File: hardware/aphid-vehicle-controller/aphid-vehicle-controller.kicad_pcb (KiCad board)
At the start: 4 copper layers, 135 parts, among them J1 MONITOR UART, J2 ModICE ME-MX 24, J3 MAIN_DEBUG, J4 MONITOR_DEBUG, U1 STM32G491CETx, U2 AMS1117-3.3, U3 LMR33630BDDA, U4 TJA1042T-3, U5 TJA1042T-3, U6 TJA1042T-3, U7 STM32G431KBTx, U8 BTS6143D, Y1 8 MHz, Y2 8 MHz

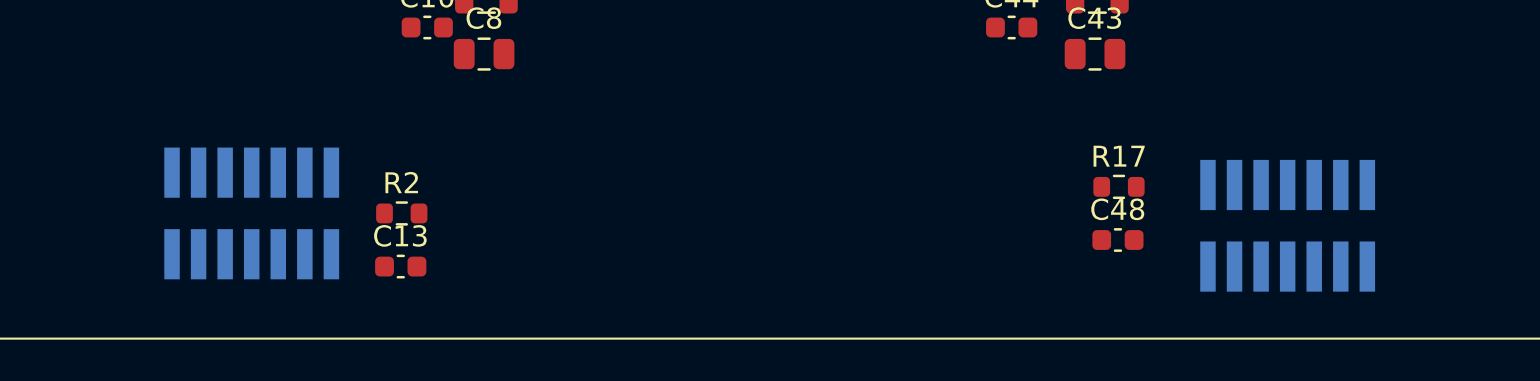
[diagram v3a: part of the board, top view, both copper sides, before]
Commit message: Changed debug connector to tagconnect
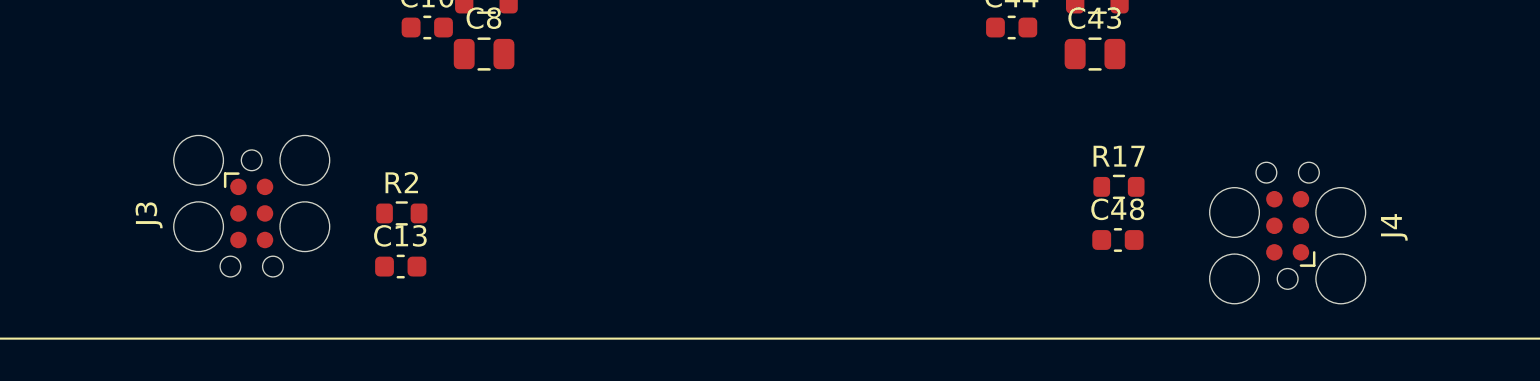
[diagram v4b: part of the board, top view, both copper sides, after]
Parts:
- J3: value MAIN_DEBUG -> SWD; footprint Connector_PinHeader_1.27mm:PinHeader_2x07_P1.27mm_Vertical_SMD -> Connector:Tag-Connect_TC2030-IDC-FP_2x03_P1.27mm_Vertical; moved to F.Cu
- J4: value MONITOR_DEBUG -> SWD; footprint Connector_PinHeader_1.27mm:PinHeader_2x07_P1.27mm_Vertical_SMD -> Connector:Tag-Connect_TC2030-IDC-FP_2x03_P1.27mm_Vertical; moved to F.Cu
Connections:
- J3 pad 1: unconnected-(J3-NC-Pad1) -> +3.3V
- J3 pad 2: unconnected-(J3-NC-Pad2) -> /MCU/MAIN_SWDIO
- J3 pad 3: +3.3V -> /MCU/MAIN_NRST
- J3 pad 4: /MCU/MAIN_SWDIO -> /MCU/MAIN_SWCLK
- J3 pad 6: /MCU/MAIN_SWCLK -> /MCU/MAIN_SWO
- J4 pad 1: unconnected-(J4-NC-Pad1) -> +3.3V
- J4 pad 2: unconnected-(J4-NC-Pad2) -> /Monitor/MONITOR_SWDIO
- J4 pad 3: +3.3V -> /Monitor/MONITOR_NRST
- J4 pad 4: /Monitor/MONITOR_SWDIO -> /Monitor/MONITOR_SWCLK
- J4 pad 6: /Monitor/MONITOR_SWCLK -> /Monitor/MONITOR_SWO
- U1 pad 22: /MCU/MAIN_DBG_TX -> unconnected-(U1-PB10-Pad22)
- U1 pad 25: /MCU/MAIN_DBG_RX -> unconnected-(U1-PB11-Pad25)

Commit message: Worked on VC PCB
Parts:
- added C15: 10 uF 50V, Capacitor_SMD:C_1206_3216Metric, F.Cu at (145.8, 51.5)
- added C19: 10 uF 50V, Capacitor_SMD:C_1206_3216Metric, F.Cu at (137.0, 70.4)
- added J4: SWD, Connector:Tag-Connect_TC2030-IDC-FP_2x03_P1.27mm_Vertical, F.Cu at (132.7, 143.5)
- added J6: SWD, Connector:Tag-Connect_TC2030-IDC-FP_2x03_P1.27mm_Vertical, F.Cu at (150.5, 143.5)
- C59: renamed from C57; value 10uF -> 10 uF 50V; footprint Capacitor_SMD:C_0805_2012Metric -> Capacitor_SMD:C_1206_3216Metric
- C60: renamed from C58; value 10uF -> 10 uF 50V; footprint Capacitor_SMD:C_0805_2012Metric -> Capacitor_SMD:C_1206_3216Metric
- C61: renamed from C59; value 10uF -> 10 uF 50V; footprint Capacitor_SMD:C_0805_2012Metric -> Capacitor_SMD:C_1206_3216Metric
- C62: renamed from C60; value 10uF -> 10 uF 50V; footprint Capacitor_SMD:C_0805_2012Metric -> Capacitor_SMD:C_1206_3216Metric
- J3: value SWD -> MAIN_DEBUG; footprint Connector:Tag-Connect_TC2030-IDC-FP_2x03_P1.27mm_Vertical -> Connector_PinHeader_1.27mm:PinHeader_2x07_P1.27mm_Vertical_SMD
- J5: renamed from J4; value SWD -> MONITOR_DEBUG; footprint Connector:Tag-Connect_TC2030-IDC-FP_2x03_P1.27mm_Vertical -> Connector_PinHeader_1.27mm:PinHeader_2x07_P1.27mm_Vertical_SMD
- R7: value 10k -> 100k
- moved C24 48.9 mm to (146.8, 133.0), turned to 180 degrees
- moved C37 44.2 mm to (149.8, 104.2)
- moved C33 44.0 mm to (148.0, 107.5)
- moved C36 42.8 mm to (146.2, 104.2), turned to 180 degrees
- moved L6 42.1 mm to (148.0, 96.8)
- moved D8 41.6 mm to (148.0, 101.2)
- moved C34 40.5 mm to (141.0, 117.2), turned to 180 degrees
- moved U5 40.0 mm to (141.0, 112.2)
- moved U4 40.0 mm to (148.0, 112.2)
- moved C40 39.2 mm to (134.0, 107.5)
- moved R8 38.8 mm to (157.8, 98.5)
- moved D3 38.8 mm to (157.8, 102.2)
- moved R9 38.2 mm to (157.8, 105.5)
- moved L7 38.2 mm to (134.0, 96.8)
- moved U2 38.1 mm to (147.8, 128.0)
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- renumbered C15 to C16, C16 to C17, C17 to C18, C18 to C20, C19 to C21, C20 to C22, C21 to C23, C22 to C24, C23 to C25, C24 to C26, C25 to C27, C26 to C28, C27 to C29, C28 to C30, C29 to C31, C30 to C32, C31 to C33, C32 to C34, C33 to C35, C34 to C36, C35 to C37, C36 to C38, C37 to C39, C38 to C40, C39 to C41, C40 to C42, C41 to C43, C42 to C44, C43 to C45, C44 to C46, C45 to C47, C46 to C48, C47 to C49, C48 to C50, C49 to C51, C50 to C52, C51 to C53, C52 to C54, C53 to C55, C54 to C56, C55 to C57, C56 to C58
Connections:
- C1 pad 1: Net-(J2A-L9) -> Net-(J2A-L3)
- C16 pad 1: +12V -> /Connectors/VIN
- C3 pad 1: Net-(J2B-R9) -> Net-(J2B-R3)
- C59 pad 1: +12V -> /Connectors/HIGH_SIDE_DRIVE
- C60 pad 1: +12V -> /Connectors/HIGH_SIDE_DRIVE
- C61 pad 1: +12V -> /Connectors/HIGH_SIDE_DRIVE
- C62 pad 1: +12V -> /Connectors/HIGH_SIDE_DRIVE
- D2 pad 1: /MCU/POWER_KEEPALIVE -> Net-(D2-Pad1)
- D2 pad 2: Net-(D2-Pad2) -> /MCU/POWER_KEEPALIVE
- J2 pad 10: /Connectors/ACC2 -> /Connectors/BRAKE2
- J2 pad 11: /Connectors/ACC1 -> /Connectors/BRAKE1
- J2 pad 14: /CAN/CAN2_LOW -> /Connectors/HIGH_SIDE_DRIVE
- J2 pad 15: /CAN/CAN2_HIGH -> Net-(J2B-R3)
- J2 pad 16: /Connectors/DIR_F2 -> /Connectors/DIR_R2
- J2 pad 17: /Connectors/DIR_F1 -> /Connectors/DIR_R1
- J2 pad 18: /Connectors/CRANK -> /Connectors/IGNITION
- J2 pad 2: /CAN/CAN1_LOW -> unconnected-(J2A-L2-Pad2)
- J2 pad 20: /Connectors/HIGH_SIDE_DRIVE -> /CAN/CAN2_LOW
- J2 pad 21: Net-(J2B-R9) -> /CAN/CAN2_HIGH
- J2 pad 22: /Connectors/DIR_R2 -> /Connectors/DIR_F2
- J2 pad 23: /Connectors/DIR_R1 -> /Connectors/DIR_F1
- J2 pad 24: /Connectors/IGNITION -> /Connectors/CRANK
- J2 pad 3: /CAN/CAN1_HIGH -> Net-(J2A-L3)
- J2 pad 4: /Connectors/BRAKE2 -> /Connectors/ACC2
- J2 pad 5: /Connectors/BRAKE1 -> /Connectors/ACC1
- J2 pad 8: unconnected-(J2A-L8-Pad8) -> /CAN/CAN1_LOW
- J2 pad 9: Net-(J2A-L9) -> /CAN/CAN1_HIGH
- J3 pad 1: +3.3V -> unconnected-(J3-NC-Pad1)
- J3 pad 2: /MCU/MAIN_SWDIO -> unconnected-(J3-NC-Pad2)
- J3 pad 3: /MCU/MAIN_NRST -> +3.3V
- J3 pad 4: /MCU/MAIN_SWCLK -> /MCU/MAIN_SWDIO
- J3 pad 6: /MCU/MAIN_SWO -> /MCU/MAIN_SWCLK
- J5 pad 1: +3.3V -> unconnected-(J5-NC-Pad1)
- J5 pad 2: /Monitor/MONITOR_SWDIO -> unconnected-(J5-NC-Pad2)
- J5 pad 3: /Monitor/MONITOR_NRST -> +3.3V
- J5 pad 4: /Monitor/MONITOR_SWCLK -> /Monitor/MONITOR_SWDIO
- J5 pad 6: /Monitor/MONITOR_SWO -> /Monitor/MONITOR_SWCLK
- L1 pad 1: Net-(J2A-L9) -> Net-(J2A-L3)
- L2 pad 1: Net-(J2B-R9) -> Net-(J2B-R3)
- R6 pad 1: Net-(D2-Pad2) -> Net-(D2-Pad1)
- U1 pad 22: unconnected-(U1-PB10-Pad22) -> /MCU/MAIN_DBG_TX
- U1 pad 25: unconnected-(U1-PB11-Pad25) -> /MCU/MAIN_DBG_RX

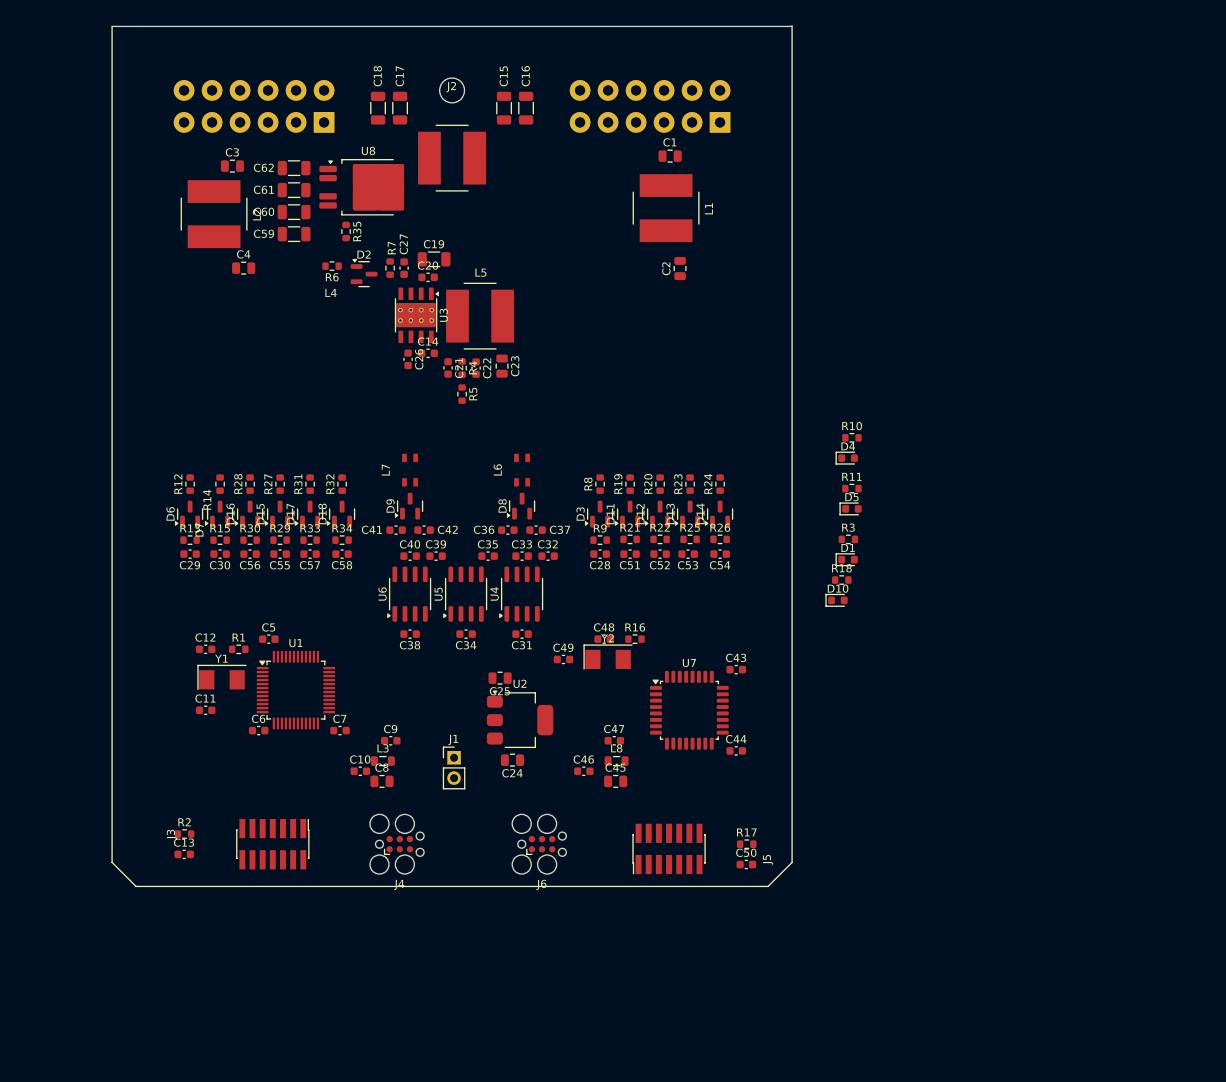
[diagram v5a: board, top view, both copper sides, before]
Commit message: Fixed some errors in ModICE footprint
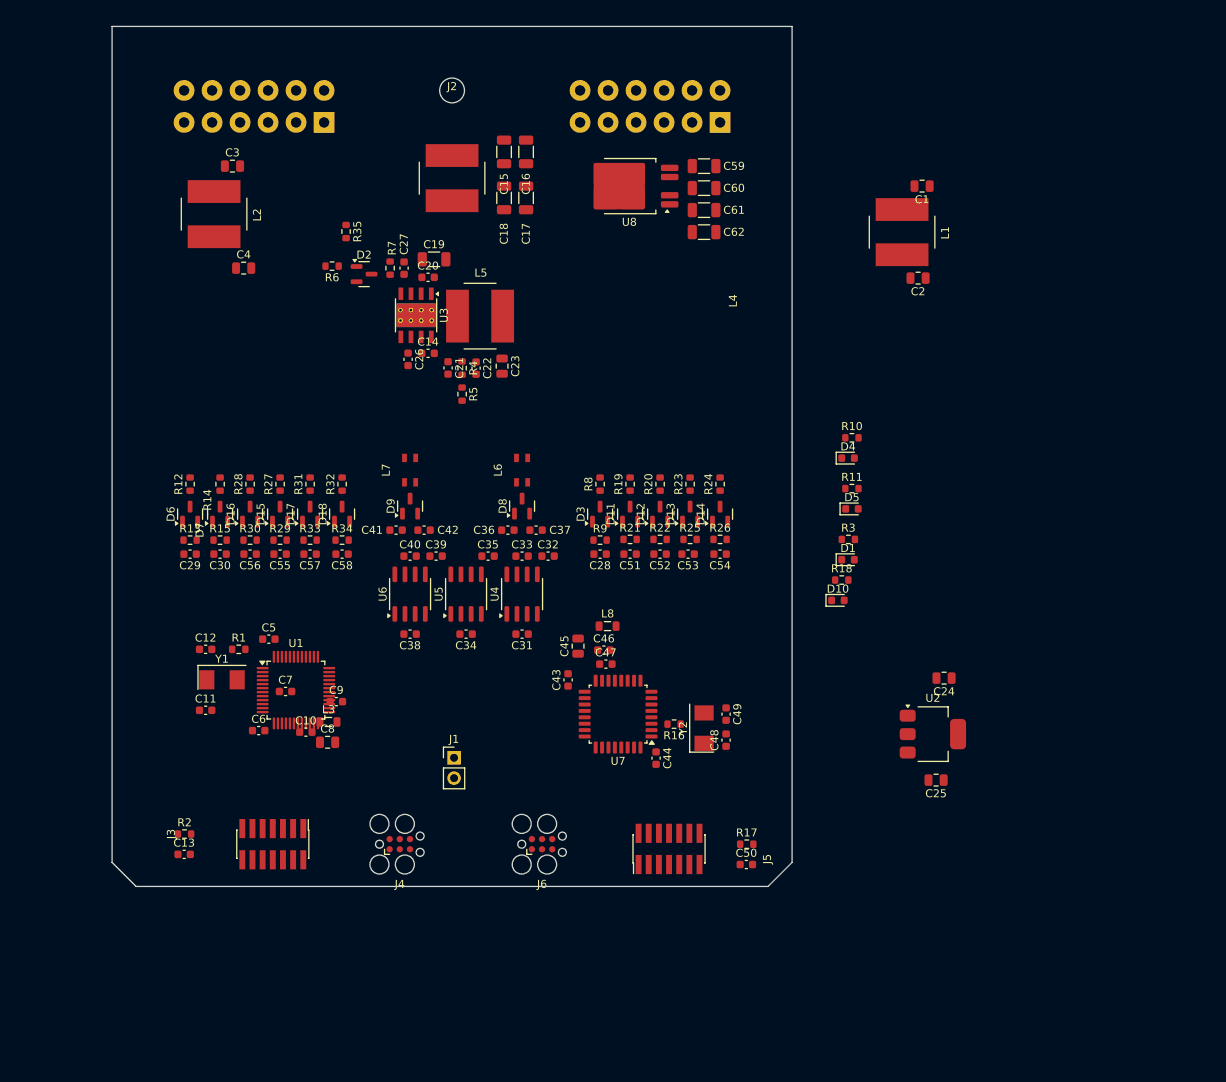
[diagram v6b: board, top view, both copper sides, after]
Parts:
- R6: value 38k -> 100k
- U2: value AMS1117-3.3 -> LD1117S33TR_SOT223
- moved C25 56.0 mm to (199.8, 135.5)
- moved C24 54.9 mm to (200.8, 122.8)
- moved C59 52.0 mm to (170.8, 58.8), turned to 0 degrees
- moved C62 51.9 mm to (170.8, 67.0), turned to 0 degrees
- moved U2 51.6 mm to (199.3, 129.8)
- moved C60 51.3 mm to (170.8, 61.5), turned to 0 degrees
- moved C61 51.3 mm to (170.8, 64.2), turned to 0 degrees
- moved U8 32.6 mm to (161.4, 61.2), turned to 180 degrees
- moved C1 31.7 mm to (198.0, 61.2), turned to 180 degrees
- moved C2 29.8 mm to (197.5, 72.8), turned to 180 degrees
- moved L1 29.7 mm to (195.5, 67.0)
- moved C49 21.4 mm to (173.5, 127.2), turned to -90 degrees
- moved C43 21.1 mm to (153.8, 123.0), turned to 90 degrees
- moved C48 19.8 mm to (173.5, 130.5), turned to 90 degrees
- moved C17 19.3 mm to (148.5, 62.7)
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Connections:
- J2 pad 14: /Connectors/HIGH_SIDE_DRIVE -> unconnected-(J2B-R2-Pad14)
- J2 pad 2: unconnected-(J2A-L2-Pad2) -> /Connectors/HIGH_SIDE_DRIVE
- U1 pad 45: unconnected-(U1-PB8-Pad45) -> /MCU/MAIN_BOOT
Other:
- board outline added: 85 x 107.5 mm

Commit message: Some cleaning up
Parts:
- removed the J3 at (116.8, 143.5)
- removed J5: MONITOR_DEBUG, Connector_PinHeader_1.27mm:PinHeader_2x07_P1.27mm_Vertical_SMD
- added JP1: MAIN_BOOT, Jumper:SolderJumper-3_P1.3mm_Bridged12_RoundedPad1.0x1.5mm, F.Cu at (126.4, 143.7)
- added JP2: MONITOR_BOOT, Jumper:SolderJumper-3_P1.3mm_Bridged12_RoundedPad1.0x1.5mm, F.Cu at (152.2, 143.5)
- J3: renamed from J4; value SWD -> MAIN_SWD
- J4: renamed from J6; value SWD -> MONITOR_SWD
- moved R3 89.4 mm to (103.2, 131.2)
- moved D1 89.4 mm to (103.0, 133.2)
- moved C25 71.6 mm to (156.8, 78.2), turned to 90 degrees
- moved U2 62.0 mm to (162.4, 80.0)
- moved C24 59.9 mm to (156.8, 82.0), turned to 90 degrees
- moved C2 44.7 mm to (153.5, 64.8), turned to -90 degrees
- moved C1 44.5 mm to (153.5, 59.2), turned to -90 degrees
- moved R35 40.1 mm to (166.0, 69.6), turned to 0 degrees
- moved D10 39.7 mm to (166.5, 146.7)
- moved R18 39.7 mm to (167.0, 144.2)
- moved L1 36.6 mm to (159.2, 62.0)
- moved C50 29.8 mm to (148.2, 135.4), turned to 180 degrees
- moved R17 28.6 mm to (148.2, 137.0), turned to 180 degrees
- moved R11 26.8 mm to (170.8, 79.6), turned to 180 degrees
- moved D5 26.5 mm to (174.4, 79.6), turned to 180 degrees
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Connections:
- J2 pad 14: unconnected-(J2B-R2-Pad14) -> GND
- J2 pad 18: /Connectors/IGNITION -> /Connectors/CRANK
- J2 pad 24: /Connectors/CRANK -> /Connectors/IGNITION
- U1 pad 10: unconnected-(U1-PA2-Pad10) -> /MCU/IGNITION_SENSE
- U1 pad 11: unconnected-(U1-PA3-Pad11) -> /MCU/CRANK_SENSE
- U1 pad 13: unconnected-(U1-PA5-Pad13) -> /Inputs/BRAKE1_FILTERED
- U1 pad 14: unconnected-(U1-PA6-Pad14) -> /Inputs/DIR_F1_FILTERED
- U1 pad 15: unconnected-(U1-PA7-Pad15) -> /Inputs/DIR_R1_FILTERED
- U1 pad 22: /MCU/MAIN_DBG_TX -> unconnected-(U1-PB10-Pad22)
- U1 pad 25: /MCU/MAIN_DBG_RX -> unconnected-(U1-PB11-Pad25)
- U1 pad 42: unconnected-(U1-PB5-Pad42) -> /MCU/MAIN_STATUS
- U1 pad 8: unconnected-(U1-PA0-Pad8) -> /Inputs/ACC1_FILTERED
- U1 pad 9: unconnected-(U1-PA1-Pad9) -> /MCU/VIN_SENSE
- U4 pad 8: unconnected-(U4-STB-Pad8) -> GND
- U7 pad 10: unconnected-(U7-PA5-Pad10) -> /Inputs/DIR_R2_FILTERED
- U7 pad 11: unconnected-(U7-PA6-Pad11) -> /High Side Out/HIGH_SIDE_ENABLE
- U7 pad 28: unconnected-(U7-PB5-Pad28) -> /Monitor/MONITOR_STATUS
- U7 pad 31: unconnected-(U7-PB8-Pad31) -> /Monitor/MONITOR_BOOT
- U7 pad 5: unconnected-(U7-PA0-Pad5) -> /Inputs/ACC2_FILTERED
- U7 pad 6: unconnected-(U7-PA1-Pad6) -> /High Side Out/HIGH_SIDE_SENSE
- U7 pad 7: /Monitor/MONITOR_DBG_TX -> /MCU/CRANK_SENSE
- U7 pad 8: /Monitor/MONITOR_DBG_RX -> /Inputs/BRAKE2_FILTERED
- U7 pad 9: unconnected-(U7-PA4-Pad9) -> /Inputs/DIR_F2_FILTERED
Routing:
- net Net-(U3-FB): track 0.00 -> 9.01 mm
- net +5V: track 0.00 -> 3.20 mm
- net GND: track 0.00 -> 2.58 mm, vias 0 -> 1
- net Net-(U3-SW): track 0.00 -> 2.15 mm
- net Net-(U3-BOOT): track 0.00 -> 2.04 mm
- net Net-(U3-VCC): track 0.00 -> 1.90 mm

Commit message: worked on vcu pcb
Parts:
- moved C59 53.3 mm to (120.8, 59.2)
- moved C60 53.3 mm to (120.8, 61.8)
- moved C62 53.3 mm to (120.8, 66.8)
- moved C61 53.2 mm to (120.8, 64.2)
- moved R35 43.2 mm to (123.5, 77.2), turned to -90 degrees
- moved U8 41.2 mm to (127.3, 71.8), turned to 0 degrees
- moved C41 33.6 mm to (109.2, 79.8)
- moved C40 32.2 mm to (113.8, 82.4)
- moved C25 31.0 mm to (132.6, 97.7)
- moved D9 30.1 mm to (114.0, 78.7)
- moved C42 29.7 mm to (117.0, 81.2)
- moved C37 29.4 mm to (167.8, 81.0), turned to 90 degrees
- moved D5 29.2 mm to (148.6, 93.2)
- moved C33 29.2 mm to (165.0, 83.8)
- moved R11 29.2 mm to (145.0, 93.2)
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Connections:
- J2 pad 14: GND -> /Connectors/HIGH_SIDE_DRIVE
- J2 pad 2: /Connectors/HIGH_SIDE_DRIVE -> GND
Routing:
- net /Connectors/HIGH_SIDE_DRIVE: track 0.00 -> 25.6 mm
- net /CAN/CAN1_LOW: track 0.00 -> 24.3 mm, vias 0 -> 1
- net /CAN/CAN2_LOW: track 0.00 -> 24.3 mm, vias 0 -> 1
- net /CAN/CAN2_HIGH: track 0.00 -> 24.2 mm, vias 0 -> 1
- net /CAN/CAN1_HIGH: track 0.00 -> 24.2 mm, vias 0 -> 1
- net GND: track 2.58 -> 21.8 mm, vias 1 -> 3
- net Net-(J2B-R3): track 0.00 -> 13.0 mm
- net +5V: track 3.20 -> 9.31 mm
- net Net-(J2A-L3): track 0.00 -> 5.92 mm
- net Net-(U3-FB): track 9.01 -> 3.62 mm
- net Net-(U3-EN): track 0.00 -> 3.74 mm
- net Net-(U3-SW): track 2.15 -> 0.00 mm
- net Net-(U3-BOOT): track 2.04 -> 0.00 mm
- net Net-(U3-VCC): track 1.90 -> 0.00 mm
- net (no net): vias 0 -> 6
- added copper zone on F.Cu, net +12V
- added copper zone on F.Cu, net /Connectors/VIN
